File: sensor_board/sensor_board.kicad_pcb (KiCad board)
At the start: 2 copper layers, 15.2 x 13.5 mm, 7 parts, among them J1 Conn_01x03, Q1 Q_Photo_NPN_EBC

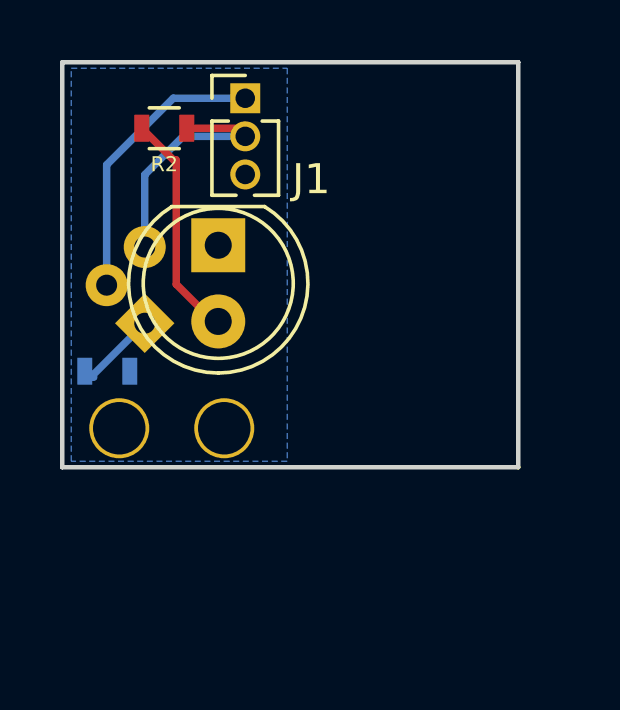
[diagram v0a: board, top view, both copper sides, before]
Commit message: redo sensor board
 - supports any combo of the two types of sensors
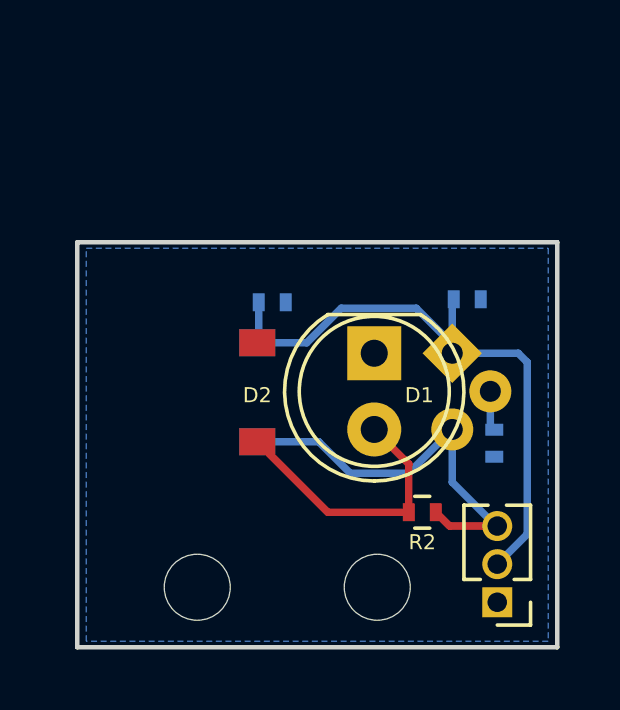
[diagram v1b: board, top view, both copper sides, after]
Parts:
- removed the REF** at (102.0, 112.2)
- removed the REF** at (105.5, 112.2)
- added D2: VSMB2943SLX01, sensor_board_custom:VSMB2943SLX01_VEMT2023SLX01, F.Cu at (106.5, 111.0)
- added Q2: VEMT2023SLX01, sensor_board_custom:VSMB2943SLX01_VEMT2023SLX01, B.Cu at (106.5, 111.0)
- added R3: 10, Resistors_SMD:R_0402, B.Cu at (114.4, 112.7)
- added R4: 619, Resistors_SMD:R_0402, B.Cu at (107.0, 108.0)
- added REF**: MountingHole_2.2mm_M2, Mounting_Holes:MountingHole_2.2mm_M2, F.Cu at (104.5, 117.5)
- added REF**: MountingHole_2.2mm_M2, Mounting_Holes:MountingHole_2.2mm_M2, F.Cu at (110.5, 117.5)
- D1: value LED -> VSLY5940
- Q1: value Q_Photo_NPN_EBC -> BPV11F
- R1: value R -> 169; footprint Resistors_SMD:R_0603 -> Resistors_SMD:R_0402
- R2: value R -> 36; footprint Resistors_SMD:R_0603 -> Resistors_SMD:R_0402
- moved J1 18.8 mm to (114.5, 118.0), turned to 180 degrees
- moved R2 15.4 mm to (112.0, 115.0)
- moved R1 12.2 mm to (113.5, 107.9)
- moved Q1 10.3 mm to (113.0, 109.7), turned to 270 degrees
- moved D1 6.32 mm to (110.4, 109.7)
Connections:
- J1 pad 1: /analog -> GND
- J1 pad 2: /5v_enable -> analog
- J1 pad 3: GND -> enable
- Q1 pad 1: Net-(Q1-Pad1) -> analog
- Q1 pad 2: /analog -> Net-(Q1-Pad2)
- Q1 pad 3: /5v_enable -> enable
- R1 pad 1: Net-(Q1-Pad1) -> analog
- R2 pad 1: /5v_enable -> enable
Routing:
- net analog: track 0.00 -> 20.4 mm
- net enable: track 0.00 -> 13.6 mm
- net /analog: track 9.55 -> 0.00 mm
- net /5v_enable: track 8.24 -> 0.00 mm
- net Net-(Q1-Pad1): track 2.70 -> 0.00 mm
- net Net-(D1-Pad2): track 7.75 -> 9.26 mm
- net Net-(Q1-Pad2): track 0.00 -> 1.33 mm
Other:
- board size 15.2 x 13.5 mm -> 16 x 13.5 mm
